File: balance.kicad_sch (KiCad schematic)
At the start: 5 parts, among them Q1 IRLML0060

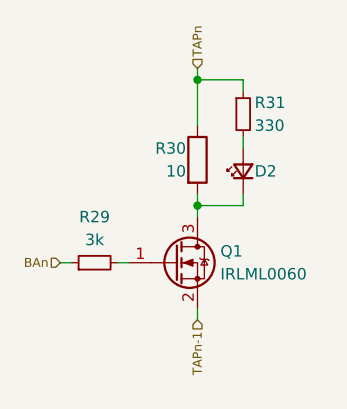
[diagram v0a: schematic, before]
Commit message: schematic: Switch to different balance resistors
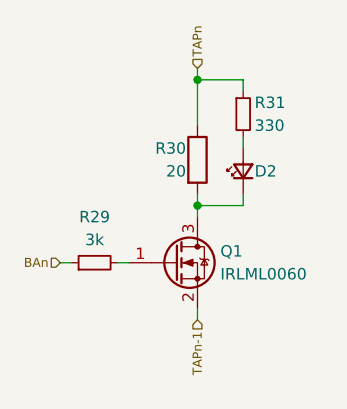
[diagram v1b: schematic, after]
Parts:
- R30: value 10 -> 20; Dist # C2991665 -> C2479206; Mfr FH -> SEI; Mfr # RPL-12K10R0FT -> RMCF2512FT20R0
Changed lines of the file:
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@@
 			)
 		)
-		(property "Value" "10"
+		(property "Value" "20"
 			(at 130.81 52.07 0)
 			(effects
@@
 			)
 		)
-		(property "Dist #" "C2991665"
+		(property "Dist #" "C2479206"
 			(at 132.08 50.8 0)
 			(effects
@@
 			)
 		)
-		(property "Mfr" "FH"
+		(property "Mfr" "SEI"
 			(at 132.08 50.8 0)
 			(effects
@@
 			)
 		)
-		(property "Mfr #" "RPL-12K10R0FT"
+		(property "Mfr #" "RMCF2512FT20R0"
 			(at 132.08 50.8 0)
 			(effects

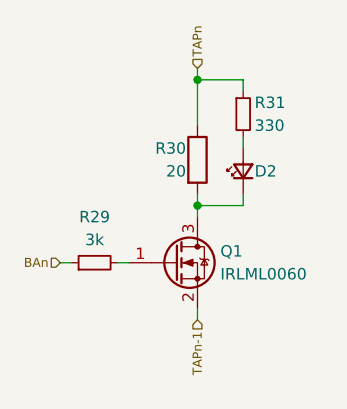
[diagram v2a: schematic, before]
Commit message: schematic: Rework thermistor frontend
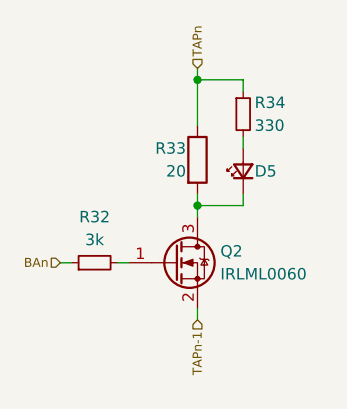
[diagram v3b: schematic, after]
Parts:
- renumbered D2 to D5, Q1 to Q2, R29 to R32, R30 to R33, R31 to R34

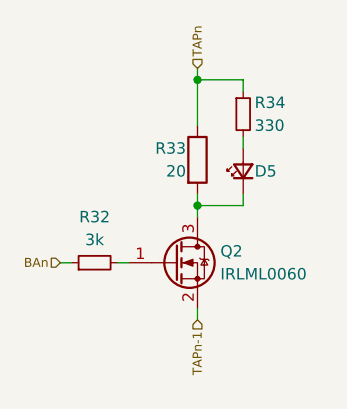
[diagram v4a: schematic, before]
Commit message: schematic: Fix-up reference designators
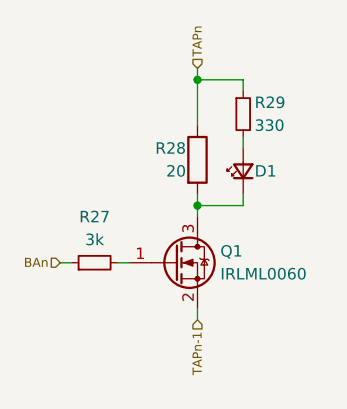
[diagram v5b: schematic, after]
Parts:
- renumbered D5 to D1, Q2 to Q1, R32 to R27, R33 to R28, R34 to R29

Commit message: schematic: Use resistor arrays for 3k resistors
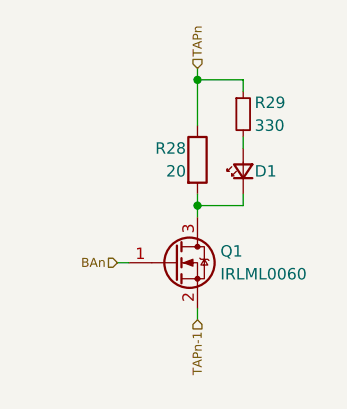
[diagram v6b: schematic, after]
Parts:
- removed R27: 3k, Resistor_SMD:R_0603_1608Metric, symbol Device:R_Small
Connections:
- net BAn: now also Q1.1 (G)
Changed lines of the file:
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@@
 	(wire
 		(pts
-			(xy 116.84 62.23) (xy 118.11 62.23)
+			(xy 123.19 62.23) (xy 124.46 62.23)
 		)
 		(stroke
@@
 	(wire
 		(pts
-			(xy 123.19 62.23) (xy 124.46 62.23)
-		)
-		(stroke
-			(width 0)
-			(type default)
-		)
-	)
-	(wire
-		(pts
 			(xy 132.08 41.91) (xy 132.08 46.99)
 		)
@@
 	(hierarchical_label "BAn"
 		(shape input)
-		(at 116.84 62.23 180)
+		(at 123.19 62.23 180)
 		(effects
 			(font
@@
 		)
 	)
-	(symbol
-		(lib_id "Device:R_Small")
-		(at 120.65 62.23 90)
-		(unit 1)
-		(exclude_from_sim no)
-		(in_bom yes)
-		(on_board yes)
-		(dnp no)
-		(fields_autoplaced yes)
-		(property "Reference" "R27"
-			(at 120.65 57.15 90)
-			(effects
-				(font
-					(size 1.27 1.27)
-				)
-			)
-		)
-		(property "Value" "3k"
-			(at 120.65 59.69 90)
-			(effects
-				(font
-					(size 1.27 1.27)
-				)
-			)
-		)
-		(property "Footprint" "Resistor_SMD:R_0603_1608Metric"
-			(at 120.65 62.23 0)
-			(effects
-				(font
-					(size 1.27 1.27)
-				)
-				(hide yes)
-			)
-		)
-		(property "Datasheet" "~"
-			(at 120.65 62.23 0)
-			(effects
-				(font
-					(size 1.27 1.27)
-				)
-				(hide yes)
-			)
-		)
-		(property "Description" "Resistor, small symbol"
-			(at 120.65 62.23 0)
-			(effects
-				(font
-					(size 1.27 1.27)
-				)
-				(hide yes)
-			)
-		)
-		(property "Dist #" "C4211"
-			(at 120.65 62.23 0)
-			(effects
-				(font
-					(size 1.27 1.27)
-				)
-				(hide yes)
-			)
-		)
-		(property "Mfr" "Uni-Royal"
-			(at 120.65 62.23 0)
-			(effects
-				(font
-					(size 1.27 1.27)
-				)
-				(hide yes)
-			)
-		)
-		(property "Mfr #" "0603WAF3001T5E"
-			(at 120.65 62.23 0)
-			(effects
-				(font
-					(size 1.27 1.27)
-				)
-				(hide yes)
-			)
-		)
-		(property "Dist" "LCSC"
-			(at 120.65 62.23 0)
-			(effects
-				(font
-					(size 1.27 1.27)
-				)
-				(hide yes)
-			)
-		)
-		(pin "1"
-		)
-		(pin "2"
-		)
-		(instances
-			(project "bms_segment"
-				(path "/ae4a7653-8e6d-4e05-b144-1e5e3b2092b7/28948f48-ac92-4ccf-aa29-40bfebbeebe0/061afbf0-38a7-4aad-9e58-d0f3974685d1"
-					(reference "R27")
-					(unit 1)
-				)
-				(path "/ae4a7653-8e6d-4e05-b144-1e5e3b2092b7/28948f48-ac92-4ccf-aa29-40bfebbeebe0/1868e0df-f8a0-46bd-9798-d286e5ba1ced"
-					(reference "R51")
-					(unit 1)
-				)
-				(path "/ae4a7653-8e6d-4e05-b144-1e5e3b2092b7/28948f48-ac92-4ccf-aa29-40bfebbeebe0/27f767ba-99fc-42f7-9230-5c46d6dfd697"
-					(reference "R39")
-					(unit 1)
-				)
-				(path "/ae4a7653-8e6d-4e05-b144-1e5e3b2092b7/28948f48-ac92-4ccf-aa29-40bfebbeebe0/4bc6a671-e3fb-4a27-8305-5f5b740fdf33"
-					(reference "R48")
-					(unit 1)
-				)
-				(path "/ae4a7653-8e6d-4e05-b144-1e5e3b2092b7/28948f48-ac92-4ccf-aa29-40bfebbeebe0/558077c3-2e79-4c16-bf32-75cbb22e7b66"
-					(reference "R57")
-					(unit 1)
-				)
-				(path "/ae4a7653-8e6d-4e05-b144-1e5e3b2092b7/28948f48-ac92-4ccf-aa29-40bfebbeebe0/5bcaf29d-feaf-497c-b526-6322a79bf7a6"
-					(reference "R54")
-					(unit 1)
-				)
-				(path "/ae4a7653-8e6d-4e05-b144-1e5e3b2092b7/28948f48-ac92-4ccf-aa29-40bfebbeebe0/5e7620f7-f0af-4745-ab5e-3fc5a156dd58"
-					(reference "R63")
-					(unit 1)
-				)
-				(path "/ae4a7653-8e6d-4e05-b144-1e5e3b2092b7/28948f48-ac92-4ccf-aa29-40bfebbeebe0/8782f8eb-ed65-45b1-bf95-5d3be5b8ad2a"
-					(reference "R72")
-					(unit 1)
-				)
-				(path "/ae4a7653-8e6d-4e05-b144-1e5e3b2092b7/28948f48-ac92-4ccf-aa29-40bfebbeebe0/8b728bd1-7ef5-48d2-bc52-73fbb8d0723f"
-					(reference "R66")
-					(unit 1)
-				)
-				(path "/ae4a7653-8e6d-4e05-b144-1e5e3b2092b7/28948f48-ac92-4ccf-aa29-40bfebbeebe0/8f62a6b1-c799-4e02-ae4e-ff12c4091a5b"
-					(reference "R30")
-					(unit 1)
-				)
-				(path "/ae4a7653-8e6d-4e05-b144-1e5e3b2092b7/28948f48-ac92-4ccf-aa29-40bfebbeebe0/99d124be-48e9-4488-ad20-ea5a08d5bdf7"
-					(reference "R69")
-					(unit 1)
-				)
-				(path "/ae4a7653-8e6d-4e05-b144-1e5e3b2092b7/28948f48-ac92-4ccf-aa29-40bfebbeebe0/a578400a-9630-406e-afcf-66a88224a81d"
-					(reference "R33")
-					(unit 1)
-				)
-				(path "/ae4a7653-8e6d-4e05-b144-1e5e3b2092b7/28948f48-ac92-4ccf-aa29-40bfebbeebe0/ae51574f-61f5-40a8-84a4-f02d08755389"
-					(reference "R60")
-					(unit 1)
-				)
-				(path "/ae4a7653-8e6d-4e05-b144-1e5e3b2092b7/28948f48-ac92-4ccf-aa29-40bfebbeebe0/b9f63902-5414-42f0-b092-c310bdd721ff"
-					(reference "R42")
-					(unit 1)
-				)
-				(path "/ae4a7653-8e6d-4e05-b144-1e5e3b2092b7/28948f48-ac92-4ccf-aa29-40bfebbeebe0/bc2a692e-3b59-4639-8552-ded9a92bfb3a"
-					(reference "R36")
-					(unit 1)
-				)
-				(path "/ae4a7653-8e6d-4e05-b144-1e5e3b2092b7/28948f48-ac92-4ccf-aa29-40bfebbeebe0/c3623945-7d17-46cb-9ed3-2ec9fb31686f"
-					(reference "R45")
-					(unit 1)
-				)
-			)
-		)
-	)

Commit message: *: Rework BOM
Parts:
- D1: Dist LCSC -> (none); Dist # C84263 -> (none); LCSC # (none) -> C84263
- Q1: DigiKey # (none) -> IRLML0060TRPBFCT-ND; Dist LCSC -> (none); Dist # C67274 -> (none); LCSC # (none) -> C67274; Mouser # (none) -> 942-IRLML0060TRPBF
- R28: DigiKey # (none) -> RMCF2512FT20R0CT-ND; Dist LCSC -> (none); Dist # C2479206 -> (none); LCSC # (none) -> C2479206; Mouser # (none) -> 708-RMCF2512FT20R0
- R29: Dist LCSC -> (none); Dist # C23138 -> (none); LCSC # (none) -> C23138
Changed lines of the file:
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@@
-			)
-		)
-		(property "Dist #" "C23138"
-			(at 137.16 45.72 0)
-			(effects
-				(font
-					(size 1.27 1.27)
-				)
-				(hide yes)
 			)
 		)
@@
 			)
 		)
-		(property "Dist" "LCSC"
+		(property "DigiKey #" ""
+			(at 137.16 45.72 0)
+			(effects
+				(font
+					(size 1.27 1.27)
+				)
+				(hide yes)
+			)
+		)
+		(property "LCSC #" "C23138"
+			(at 137.16 45.72 0)
+			(effects
+				(font
+					(size 1.27 1.27)
+				)
+				(hide yes)
+			)
+		)
+		(property "Mouser #" ""
 			(at 137.16 45.72 0)
 			(effects
@@
 			)
 		)
-		(property "Dist #" "C2479206"
-			(at 132.08 50.8 0)
-			(effects
-				(font
-					(size 1.27 1.27)
-				)
-				(hide yes)
-			)
-		)
 		(property "Mfr" "SEI"
 			(at 132.08 50.8 0)
@@
 			)
 		)
-		(property "Dist" "LCSC"
+		(property "DigiKey #" "RMCF2512FT20R0CT-ND"
+			(at 132.08 50.8 0)
+			(effects
+				(font
+					(size 1.27 1.27)
+				)
+				(hide yes)
+			)
+		)
+		(property "LCSC #" "C2479206"
+			(at 132.08 50.8 0)
+			(effects
+				(font
+					(size 1.27 1.27)
+				)
+				(hide yes)
+			)
+		)
+		(property "Mouser #" "708-RMCF2512FT20R0"
 			(at 132.08 50.8 0)
 			(effects
@@
 			)
 		)
-		(property "Dist #" "C84263"
-			(at 137.16 52.07 0)
-			(effects
-				(font
-					(size 1.27 1.27)
-				)
-				(hide yes)
-			)
-		)
 		(property "Mfr" "Foshan NationStar Optoelectronics"
 			(at 137.16 52.07 0)
@@
 			)
 		)
-		(property "Dist" "LCSC"
-			(at 137.16 52.07 0)
-			(effects
-				(font
-					(size 1.27 1.27)
-				)
-				(hide yes)
-			)
-		)
 		(property "Sim.Pin" "1=K 2=A"
 			(at 137.16 52.07 0)
@@
 		(property "Sim.Pins" "1=K 2=A"
 			(at 137.16 52.07 0)
+			(effects
+				(font
+					(size 1.27 1.27)
+				)
+				(hide yes)
+			)
+		)
+		(property "DigiKey #" ""
+			(at 137.16 52.07 90)
+			(effects
+				(font
+					(size 1.27 1.27)
+				)
+				(hide yes)
+			)
+		)
+		(property "LCSC #" "C84263"
+			(at 137.16 52.07 90)
+			(effects
+				(font
+					(size 1.27 1.27)
+				)
+				(hide yes)
+			)
+		)
+		(property "Mouser #" ""
+			(at 137.16 52.07 90)
 			(effects
 				(font
@@
 			)
 		)
-		(property "Dist #" "C67274"
-			(at 129.54 62.23 0)
-			(effects
-				(font
-					(size 1.27 1.27)
-				)
-				(hide yes)
-			)
-		)
 		(property "Mfr" "Infineon"
 			(at 129.54 62.23 0)
@@
 			)
 		)
-		(property "Dist" "LCSC"
+		(property "DigiKey #" "IRLML0060TRPBFCT-ND"
 			(at 129.54 62.23 0)
 			(effects
+				(font
+					(size 1.27 1.27)
+				)
+				(hide yes)
+			)
+		)
+		(property "LCSC #" "C67274"
+			(at 129.54 62.23 0)
+			(effects
+				(font
+					(size 1.27 1.27)
+				)
+				(hide yes)
+			)
+		)
+		(property "Mouser #" "942-IRLML0060TRPBF"
+			(at 129.54 62.23 0)
+			(effects
